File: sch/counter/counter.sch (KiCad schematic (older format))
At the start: 15 parts, among them J1 CLK, J11 ~RST, J2 Carry, J3 Power, J4 Q

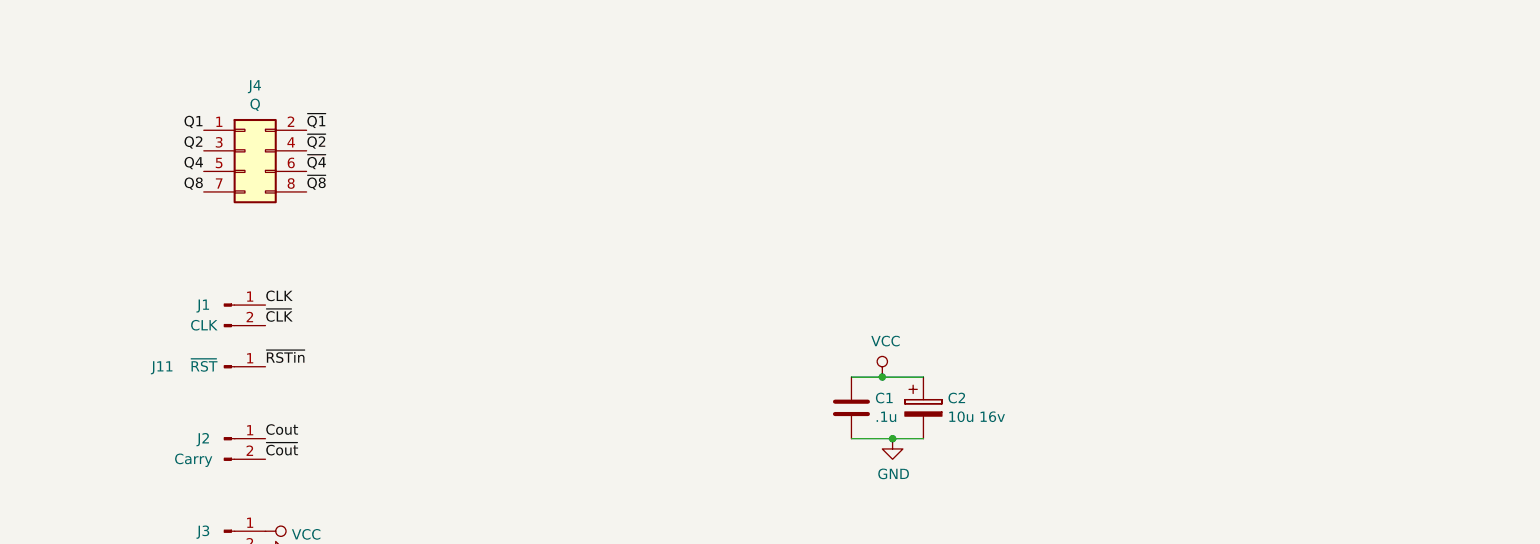
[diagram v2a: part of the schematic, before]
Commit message: Modified the counter board
Added mounting holes to the schematics
Changed reset connector to have 2 pins
Added labels for connectors and configuration diodes
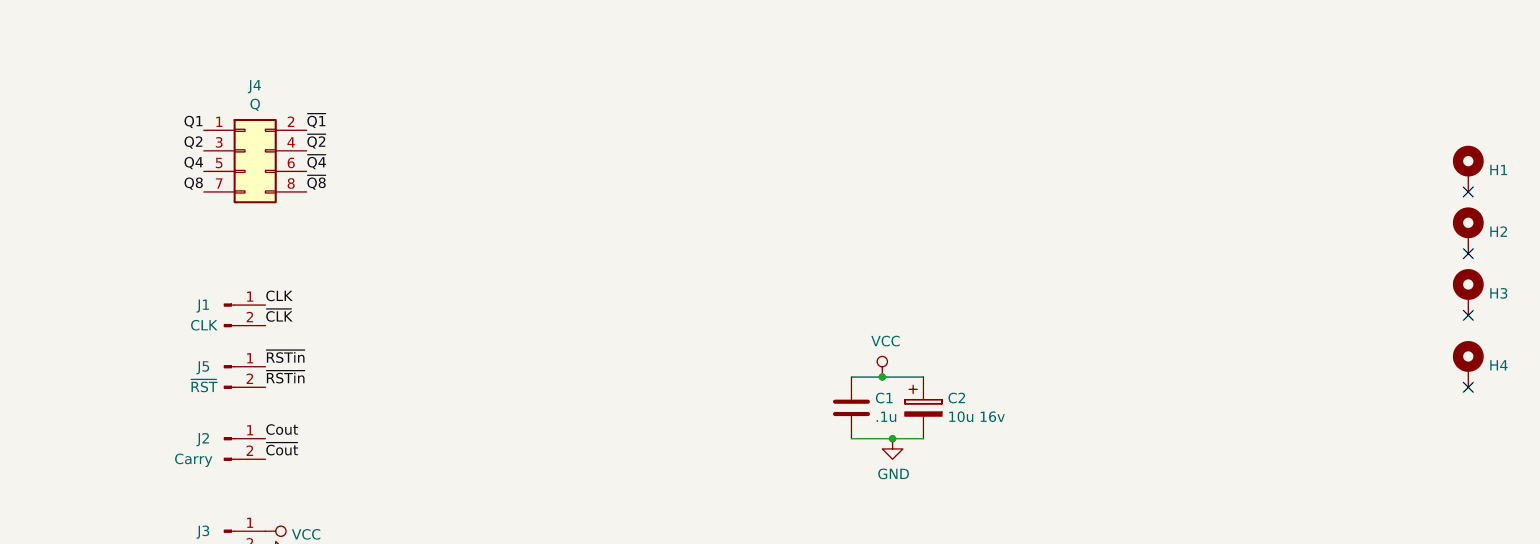
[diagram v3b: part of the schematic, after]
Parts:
- removed J11: ~RST, Connector_Pin:Pin_D1.0mm_L10.0mm, symbol Connector:Conn_01x01_Male
- added H1, H2, H3, H4: MountingHole_Pad, MountingHole:MountingHole_3.2mm_M3_DIN965_Pad, symbol Mechanical:MountingHole_Pad
- added J5: ~RST, Connector_PinHeader_2.54mm:PinHeader_1x02_P2.54mm_Vertical, symbol Connector:Conn_01x02_Male
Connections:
- net ~RSTin: now also J5.1 (Pin_1), J5.2 (Pin_2)
- no-connect marks 0 -> 4
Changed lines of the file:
@@
 Text Label 4950 4150 0    50   ~ 0
 ~CLK
-$Comp
-L Connector:Conn_01x01_Male J11
-U 1 1 5BF7CFCF
-P 4750 4350
-F 0 "J11" H 4450 4350 50  0000 C CNN
-F 1 "~RST" H 4650 4350 50  0000 C CNN
-F 2 "Connector_Pin:Pin_D1.0mm_L10.0mm" H 4750 4350 50  0001 C CNN
-F 3 "~" H 4750 4350 50  0001 C CNN
-	1    4750 4350
-	1    0    0    -1
-$EndComp
 Text Label 4950 4350 0    50   ~ 0
 ~RSTin
@@
 	1    0    0    -1
 $EndComp
+$Comp
+L Mechanical:MountingHole_Pad H1
+U 1 1 5C11CC62
+P 10800 3400
+F 0 "H1" H 10900 3405 50  0000 L CNN
+F 1 "MountingHole_Pad" H 10900 3360 50  0001 L CNN
+F 2 "MountingHole:MountingHole_3.2mm_M3_DIN965_Pad" H 10800 3400 50  0001 C CNN
+F 3 "~" H 10800 3400 50  0001 C CNN
+	1    10800 3400
+	1    0    0    -1
+$EndComp
+NoConn ~ 10800 3500
+$Comp
+L Mechanical:MountingHole_Pad H2
+U 1 1 5C11D0D6
+P 10800 3700
+F 0 "H2" H 10900 3705 50  0000 L CNN
+F 1 "MountingHole_Pad" H 10900 3660 50  0001 L CNN
+F 2 "MountingHole:MountingHole_3.2mm_M3_DIN965_Pad" H 10800 3700 50  0001 C CNN
+F 3 "~" H 10800 3700 50  0001 C CNN
+	1    10800 3700
+	1    0    0    -1
+$EndComp
+NoConn ~ 10800 3800
+$Comp
+L Mechanical:MountingHole_Pad H3
+U 1 1 5C11D35C
+P 10800 4000
+F 0 "H3" H 10900 4005 50  0000 L CNN
+F 1 "MountingHole_Pad" H 10900 3960 50  0001 L CNN
+F 2 "MountingHole:MountingHole_3.2mm_M3_DIN965_Pad" H 10800 4000 50  0001 C CNN
+F 3 "~" H 10800 4000 50  0001 C CNN
+	1    10800 4000
+	1    0    0    -1
+$EndComp
+NoConn ~ 10800 4100
+$Comp
+L Mechanical:MountingHole_Pad H4
+U 1 1 5C11D5E3
+P 10800 4350
+F 0 "H4" H 10900 4355 50  0000 L CNN
+F 1 "MountingHole_Pad" H 10900 4310 50  0001 L CNN
+F 2 "MountingHole:MountingHole_3.2mm_M3_DIN965_Pad" H 10800 4350 50  0001 C CNN
+F 3 "~" H 10800 4350 50  0001 C CNN
+	1    10800 4350
+	1    0    0    -1
+$EndComp
+NoConn ~ 10800 4450
+Text Label 4950 4450 0    50   ~ 0
+~RSTin
+$Comp
+L Connector:Conn_01x02_Male J5
+U 1 1 5C11F53F
+P 4750 4350
+F 0 "J5" H 4650 4350 50  0000 C CNN
+F 1 "~RST" H 4650 4250 50  0000 C CNN
+F 2 "Connector_PinHeader_2.54mm:PinHeader_1x02_P2.54mm_Vertical" H 4750 4350 50  0001 C CNN
+F 3 "~" H 4750 4350 50  0001 C CNN
+	1    4750 4350
+	1    0    0    -1
+$EndComp

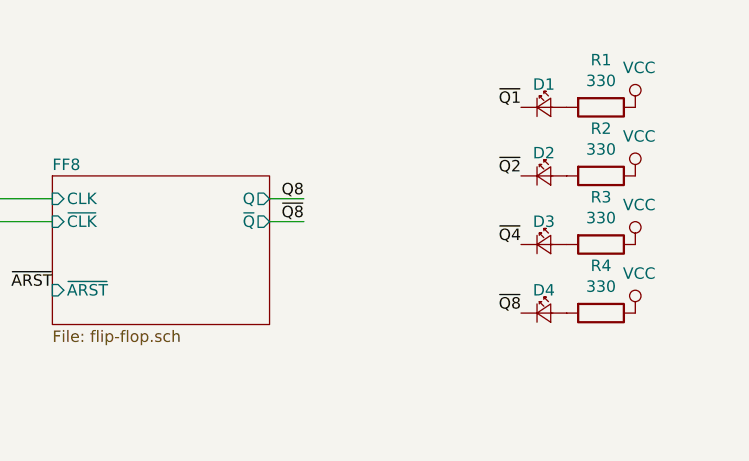
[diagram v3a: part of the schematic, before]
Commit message: Added datasheets, set component values, calculated LED resistors
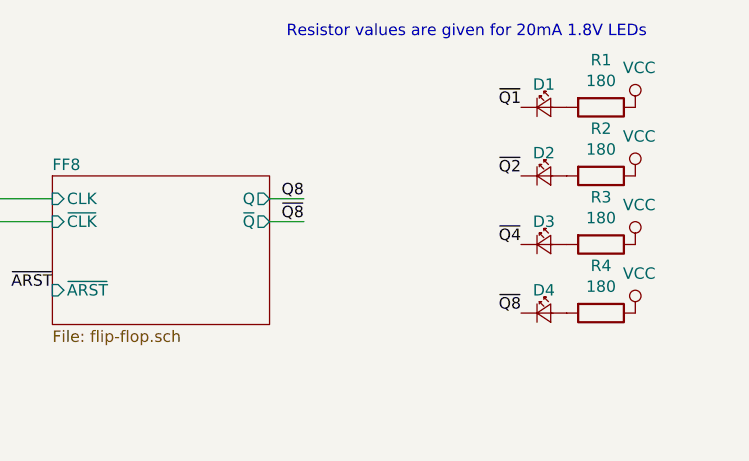
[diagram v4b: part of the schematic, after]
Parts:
- R1, R2, R3, R4: value 330 -> 180
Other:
- note added: "Resistor values are given for 20mA 1.8V LEDs"
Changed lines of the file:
@@
 P 10500 1350
 F 0 "R1" V 10293 1350 50  0000 C CNN
-F 1 "330" V 10384 1350 50  0000 C CNN
+F 1 "180" V 10384 1350 50  0000 C CNN
 F 2 "Resistor_SMD:R_0805_2012Metric" V 10430 1350 50  0001 C CNN
 F 3 "~" H 10500 1350 50  0001 C CNN
@@
 P 10500 1650
 F 0 "R2" V 10293 1650 50  0000 C CNN
-F 1 "330" V 10384 1650 50  0000 C CNN
+F 1 "180" V 10384 1650 50  0000 C CNN
 F 2 "Resistor_SMD:R_0805_2012Metric" V 10430 1650 50  0001 C CNN
 F 3 "~" H 10500 1650 50  0001 C CNN
@@
 P 10500 1950
 F 0 "R3" V 10293 1950 50  0000 C CNN
-F 1 "330" V 10384 1950 50  0000 C CNN
+F 1 "180" V 10384 1950 50  0000 C CNN
 F 2 "Resistor_SMD:R_0805_2012Metric" V 10430 1950 50  0001 C CNN
 F 3 "~" H 10500 1950 50  0001 C CNN
@@
 P 10500 2250
 F 0 "R4" V 10293 2250 50  0000 C CNN
-F 1 "330" V 10384 2250 50  0000 C CNN
+F 1 "180" V 10384 2250 50  0000 C CNN
 F 2 "Resistor_SMD:R_0805_2012Metric" V 10430 2250 50  0001 C CNN
 F 3 "~" H 10500 2250 50  0001 C CNN
@@
 	1    0    0    -1
 $EndComp
+Text Notes 10700 1050 2    50   ~ 0
+Resistor values are given for 20mA 1.8V LEDs
 $EndSCHEMATC
